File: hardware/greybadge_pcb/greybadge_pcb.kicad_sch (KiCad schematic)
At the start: 71 parts, among them J1 Conn_02x05_Row_Letter_First, J2 Conn_02x05_Row_Letter_First, J3 Conn_02x05_Row_Letter_First, J4 Conn_02x05_Row_Letter_First, SW1 SW_Push, SW2 SW_Push, SW3 SW_Push, SW4 SW_Push, SW5 SW_Push, SW6 SW_Push, SW7 SW_Push, U1 TLV62568DBV, U2 TLV62568DBV, U3 TLV73325PDBV

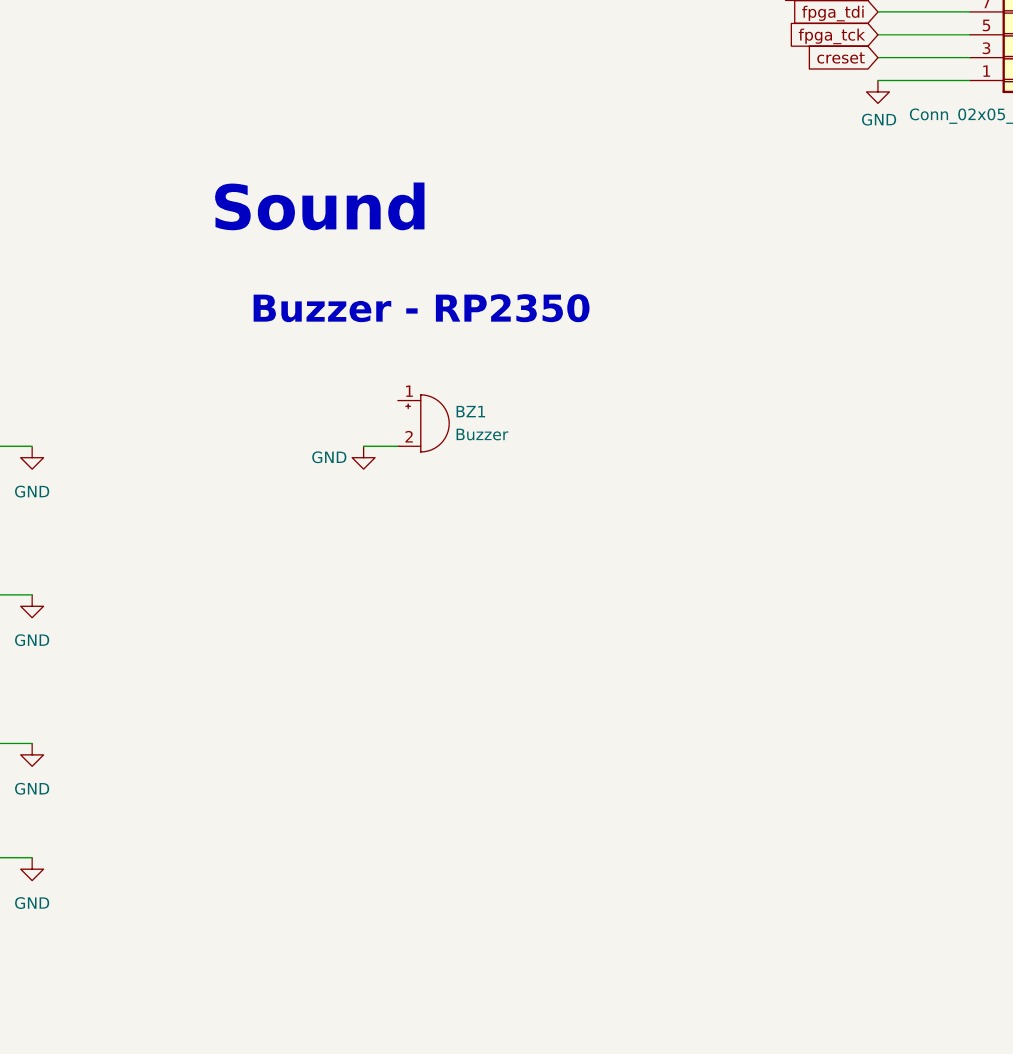
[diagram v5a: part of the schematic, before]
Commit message: feat: oled move to top sch
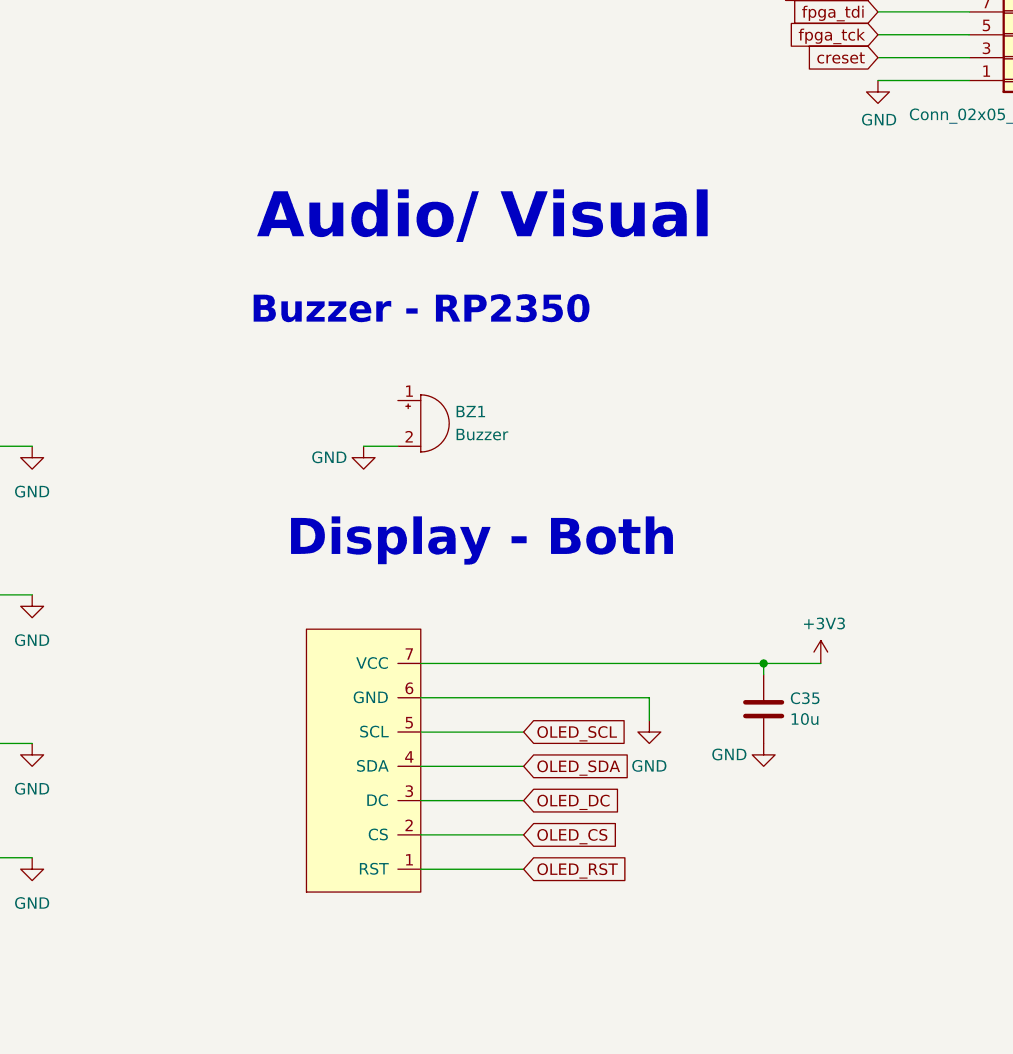
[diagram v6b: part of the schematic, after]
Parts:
- added C35: 10u, Capacitor_SMD:C_0402_1005Metric, symbol Device:C
- added GC9A1: CG9A01, custom:GC9A01, symbol maimai:CG9A01
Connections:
- net +3V3: now also C35.1, GC9A1.7 (VCC)
- net GND: now also C35.2, GC9A1.6 (GND)
- new net OLED_CS: GC9A1.2 (CS)
- new net OLED_DC: GC9A1.3 (DC)
- new net OLED_RST: GC9A1.1 (RST)
- new net OLED_SCL: GC9A1.5 (SCL)
- new net OLED_SDA: GC9A1.4 (SDA)
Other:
- note added: "Audio/ Visual"
- note added: "Display - Both"
- note removed: "Sound"

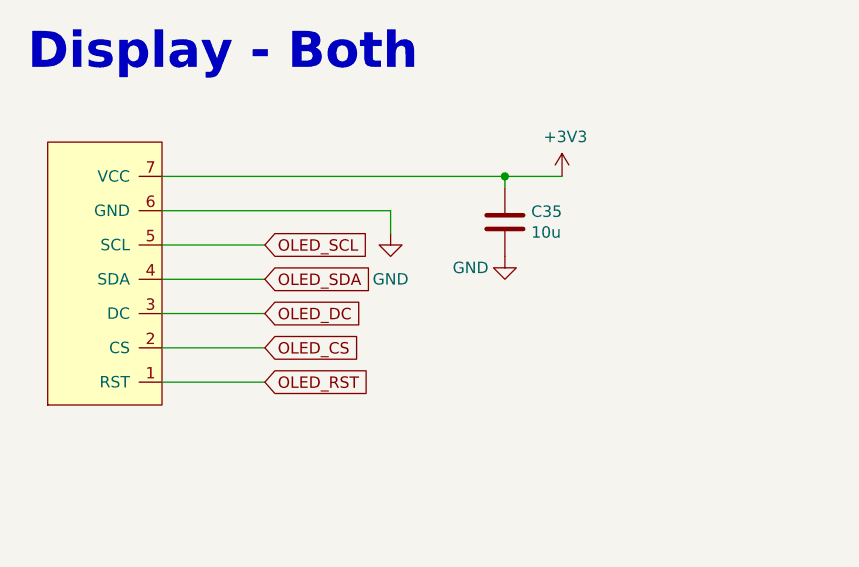
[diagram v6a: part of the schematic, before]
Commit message: feat: oled to fpga
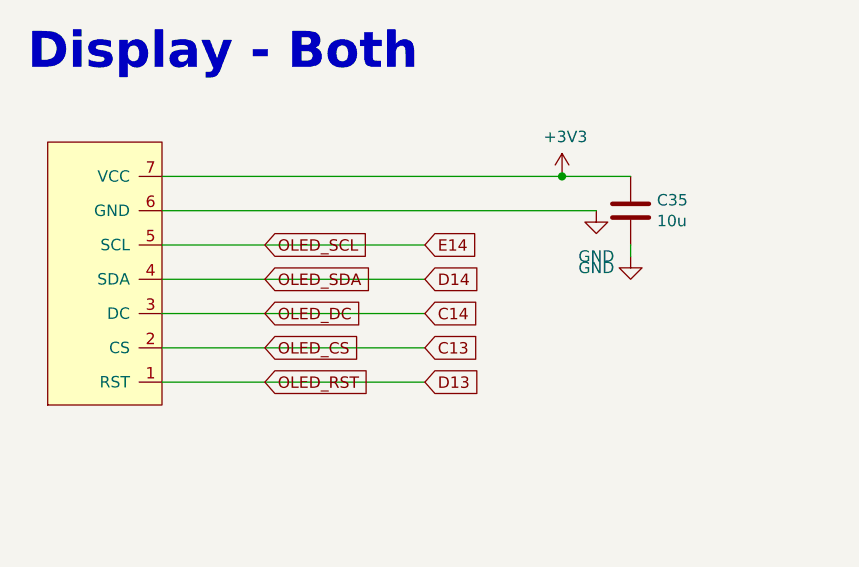
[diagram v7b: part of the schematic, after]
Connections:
- net OLED_CS renamed C13
- net OLED_DC renamed C14
- net OLED_RST renamed D13
- net OLED_SCL renamed E14
- net OLED_SDA renamed D14
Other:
- moved on the sheet: C35
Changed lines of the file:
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@@
 	)
 	(junction
+		(at 347.98 130.81)
+		(diameter 0)
+		(color 0 0 0 0)
+	)
+	(junction
 		(at 161.29 212.09)
 		(diameter 0)
@@
 	)
 	(junction
-		(at 341.63 130.81)
-		(diameter 0)
-		(color 0 0 0 0)
-	)
-	(junction
 		(at 77.47 147.32)
 		(diameter 0)
@@
 	(wire
 		(pts
-			(xy 303.53 134.62) (xy 328.93 134.62)
+			(xy 303.53 134.62) (xy 351.79 134.62)
 		)
 		(stroke
@@
 	(wire
 		(pts
-			(xy 303.53 146.05) (xy 314.96 146.05)
+			(xy 303.53 146.05) (xy 332.74 146.05)
 		)
 		(stroke
@@
 	(wire
 		(pts
-			(xy 303.53 142.24) (xy 314.96 142.24)
+			(xy 303.53 142.24) (xy 332.74 142.24)
 		)
 		(stroke
@@
 	(wire
 		(pts
-			(xy 303.53 153.67) (xy 314.96 153.67)
+			(xy 303.53 153.67) (xy 332.74 153.67)
 		)
 		(stroke
@@
 	(wire
 		(pts
-			(xy 341.63 130.81) (xy 347.98 130.81)
+			(xy 247.65 139.7) (xy 248.92 139.7)
 		)
 		(stroke
@@
 	(wire
 		(pts
-			(xy 247.65 139.7) (xy 248.92 139.7)
+			(xy 100.33 264.16) (xy 102.87 264.16)
 		)
 		(stroke
@@
 	(wire
 		(pts
-			(xy 100.33 264.16) (xy 102.87 264.16)
+			(xy 208.28 54.61) (xy 220.98 54.61)
 		)
 		(stroke
@@
 	(wire
 		(pts
-			(xy 208.28 54.61) (xy 220.98 54.61)
+			(xy 355.6 130.81) (xy 347.98 130.81)
 		)
 		(stroke
@@
 	(wire
 		(pts
-			(xy 303.53 149.86) (xy 314.96 149.86)
+			(xy 303.53 149.86) (xy 332.74 149.86)
 		)
 		(stroke
@@
 	(wire
 		(pts
-			(xy 303.53 138.43) (xy 314.96 138.43)
+			(xy 303.53 138.43) (xy 332.74 138.43)
 		)
 		(stroke
@@
 	(wire
 		(pts
-			(xy 328.93 134.62) (xy 328.93 137.16)
-		)
-		(stroke
-			(width 0)
-			(type default)
-		)
-	)
-	(wire
-		(pts
 			(xy 102.87 266.7) (xy 100.33 266.7)
 		)
@@
 	(wire
 		(pts
-			(xy 341.63 132.08) (xy 341.63 130.81)
+			(xy 45.72 241.3) (xy 59.69 241.3)
 		)
 		(stroke
@@
 	(wire
 		(pts
-			(xy 45.72 241.3) (xy 59.69 241.3)
+			(xy 355.6 138.43) (xy 355.6 139.7)
 		)
 		(stroke
@@
 	(wire
 		(pts
-			(xy 303.53 130.81) (xy 341.63 130.81)
+			(xy 303.53 130.81) (xy 347.98 130.81)
 		)
 		(stroke
@@
 			"dwBLAGgAVABKAHYAOABPAFgAeQBkAHgARQAyAHYARAAwAHcAYwBPAGoAegA3AHEAQgBnADgAdQBJ"
 			"AFQAZABBAHcAaQB3AGwAQQBMAGwAeABJAEkAawA4AEEARQBnAGoAYgBOAGIAdwB2AFEAYQB4AGkA"
-			"bQBoAEIAMwBEAFMAeQB2AHUAQQBnAGEAeAAvAE4AMwBiAEIAWABZADAAcQBIAHMAcwB5AA=="
+			"bQBoAEIAMwBEAFMAeQB2AHUAQQBnAGEAeAAvAE4AMwBiAEIAWABZADAAcQBIAHMAcwB5AGwAOQBh"
+			"AHEAUABiAFIAagBGAFYAQgBBADAAUgAyAEcAMgBvAGsAdwBMADQAcwBZAGEASAAxAE8ARABpAHcA"
+			"ZQBKAGgAaQBHAHgATQBVAEYANwBZAG8AQwBOAFEARQBpAGMARQBTAEYAQQBDAEEANABNAGcAcgBX"
+			"AHAAZwBXAGIAQwBMAGsAcwBNAHEAUQBNAHIAQQBsACsAagBqAFkANQB2AC8AVQBrAHMAWQBPAFEA"
+			"TwBBAGgAbABGAGIAYgA3AFYAQgBlAEUAWQB4AHYARABQAEQAUwBGAG4ARgByADUAKwBOAHIARgB6"
+			"AGkARwBmAFkAbgA4AEsASABzAEkANwBlADEARgB0AGYAdgBGAE8AaAA3AGgARQBDAGkAUwAxAGwA"
+			"TABSACsAKwA2AHQAWgBuADMAMwBqAHEAMQBlADMAcgBIAG4AMwA4ADAAVgBKAFUAbgB0AFkAegAr"
+			"AGMAcgB6AHIANQA1AC8AKwByAGwAbAB0AEIAaABHAFoANgBsAGoAMQBzAFEAegBXADkAQQBtAHUA"
+			"VQArAE0AcABUAHgAcwBVAGcAQgA0ADgAYgA2AHUATABmAG4ARQBQAE0AMwBLAGEARwBFAFgAbABi"
+			"AGoAOQBpAGgAWAB2AEcAOQAvAFYAdgBmAGIAMQB0AGYAZgBjAGUAOQArADQAdABvADcARgBjADUA"
+			"YQB1AG0ASAA5ACsAVgA5AEwATgA4AEkATgA1AGIAeAA0AE4ATwAwADEAagBqAE0AUQBBAFIAdQB4"
+			"AHAASABUAFAASwAxAFoAYgBCAHQATgA3AEsAUwBRAGoAaQBpAHMARgBOAEsARABJAHgAZwAyAHcA"
+			"ZQBrAFMAZABXAE4AcgA0AFMATQBmADcARgBCAHoALwA5AHgATABwAEgAMQBtADkAZQB2ACsANwBG"
+			"AHQAUgBQAGIAdQBpACsANwA0AEsAbwBsAHMAMQBlAHEAMAA3AG8AZAByAEsARgBmAGIASQB0AFQA"
+			"cwBjAFUASQBKAGkAUgAyAC8AdABSAHoAKwBDAEoAOQAvAG8AVgBuADcAcgAvAG4AdgBpAGwAVABw"
+			"AG4AegBnAGYAVABlAHYAZQBmAG8ARgBxAHAAVwBxADMATgBhAGEAdABKAC8AZQBmAFIAYgA1AEoA"
+			"TgBjADgANABpAGkAVwBaAE0ANgBVAHUAZQBOAGIASgBwAFIAUQBzAGEAbwBmAHYAKwBIAGoAZAB6"
+			"AC8AOAB2AGIAdQAvADkAMAA5AEoAYQAzAFgAdQAyAFcAZQAxAGwAOABaAE4AcQBFADYAeABYAEoA"
+			"SABDAE4AVQA4AEEARwBPAEgAVABKADgANQBOADAANQBRAGsASQBoAE4AQgBQAE8AQgBEAA=="
 		)
 	)
@@
 		)
 	)
+	(global_label "E14"
+		(shape input)
+		(at 332.74 138.43 0)
+		(fields_autoplaced yes)
+		(effects
+			(font
+				(size 1.27 1.27)
+			)
+			(justify left)
+		)
+		(property "Intersheetrefs" "${INTERSHEET_REFS}"
+			(at 339.2932 138.43 0)
+			(effects
+				(font
+					(size 1.27 1.27)
+				)
+				(justify left)
+				(hide yes)
+			)
+		)
+	)
 	(global_label "GPIO14"
 		(shape input)
@@
 		)
 	)
+	(global_label "C13"
+		(shape input)
+		(at 332.74 149.86 0)
+		(fields_autoplaced yes)
+		(effects
+			(font
+				(size 1.27 1.27)
+			)
+			(justify left)
+		)
+		(property "Intersheetrefs" "${INTERSHEET_REFS}"
+			(at 339.4142 149.86 0)
+			(effects
+				(font
+					(size 1.27 1.27)
+				)
+				(justify left)
+				(hide yes)
+			)
+		)
+	)
 	(global_label "B11"
 		(shape input)
@@
 		)
 	)
+	(global_label "D13"
+		(shape input)
+		(at 332.74 153.67 0)
+		(fields_autoplaced yes)
+		(effects
+			(font
+				(size 1.27 1.27)
+			)
+			(justify left)
+		)
+		(property "Intersheetrefs" "${INTERSHEET_REFS}"
+			(at 339.4142 153.67 0)
+			(effects
+				(font
+					(size 1.27 1.27)
+				)
+				(justify left)
+				(hide yes)
+			)
+		)
+	)
 	(global_label "B9"
 		(shape input)
@@
 		)
 	)
+	(global_label "D14"
+		(shape input)
+		(at 332.74 142.24 0)
+		(fields_autoplaced yes)
+		(effects
+			(font
+				(size 1.27 1.27)
+			)
+			(justify left)
+		)
+		(property "Intersheetrefs" "${INTERSHEET_REFS}"
+			(at 339.4142 142.24 0)
+			(effects
+				(font
+					(size 1.27 1.27)
+				)
+				(justify left)
+				(hide yes)
+			)
+		)
+	)
 	(global_label "GPIO13"
 		(shape input)
@@
 		)
 	)
+	(global_label "C14"
+		(shape input)
+		(at 332.74 146.05 0)
+		(fields_autoplaced yes)
+		(effects
+			(font
+				(size 1.27 1.27)
+			)
+			(justify left)
+		)
+		(property "Intersheetrefs" "${INTERSHEET_REFS}"
+			(at 339.4142 146.05 0)
+			(effects
+				(font
+					(size 1.27 1.27)
+				)
+				(justify left)
+				(hide yes)
+			)
+		)
+	)
 	(global_label "C3"
 		(shape input)
@@
 	(symbol
 		(lib_id "power:GND")
-		(at 328.93 137.16 0)
+		(at 351.79 134.62 0)
 		(unit 1)
 		(exclude_from_sim no)
@@
 		(fields_autoplaced yes)
 		(property "Reference" "#PWR096"
-			(at 328.93 143.51 0)
+			(at 351.79 140.97 0)
 			(effects
 				(font
@@
 		)
 		(property "Value" "GND"
-			(at 328.93 142.24 0)
+			(at 351.79 139.7 0)
 			(effects
 				(font
@@
 		)
 		(property "Footprint" ""
-			(at 328.93 137.16 0)
+			(at 351.79 134.62 0)
 			(effects
 				(font
@@
 		)
 		(property "Datasheet" ""
-			(at 328.93 137.16 0)
+			(at 351.79 134.62 0)
 			(effects
 				(font
@@
 		)
 		(property "Description" ""
-			(at 328.93 137.16 0)
+			(at 351.79 134.62 0)
 			(effects
 				(font
@@
 	(symbol
 		(lib_id "Device:C")
-		(at 341.63 135.89 0)
+		(at 355.6 134.62 0)
 		(unit 1)
 		(exclude_from_sim no)
@@
 		(dnp no)
 		(property "Reference" "C35"
-			(at 344.551 134.7216 0)
+			(at 358.521 133.4516 0)
 			(effects
 				(font
@@
 		)
 		(property "Value" "10u"
-			(at 344.551 137.033 0)
+			(at 358.521 135.763 0)
 			(effects
 				(font
@@
 		)
 		(property "Footprint" "Capacitor_SMD:C_0402_1005Metric"
-			(at 342.5952 139.7 0)
+			(at 356.5652 138.43 0)
 			(effects
 				(font
@@
 		)
 		(property "Datasheet" "~"
-			(at 341.63 135.89 0)
+			(at 355.6 134.62 0)
 			(effects
 				(font
@@
 		)
 		(property "Description" ""
-			(at 341.63 135.89 0)
+			(at 355.6 134.62 0)
 			(effects
 				(font
@@
 	(symbol
 		(lib_id "power:GND")
-		(at 341.63 139.7 0)
+		(at 355.6 139.7 0)
 		(unit 1)
 		(exclude_from_sim no)
@@
 		(dnp no)
 		(property "Reference" "#PWR097"
-			(at 341.63 146.05 0)
+			(at 355.6 146.05 0)
 			(effects
 				(font
@@
 		)
 		(property "Value" "GND"
-			(at 337.82 140.97 0)
+			(at 351.79 140.97 0)
 			(effects
 				(font
@@
 		)
 		(property "Footprint" ""
-			(at 341.63 139.7 0)
+			(at 355.6 139.7 0)
 			(effects
 				(font
@@
 		)
 		(property "Datasheet" ""
-			(at 341.63 139.7 0)
+			(at 355.6 139.7 0)
 			(effects
 				(font
@@
 		)
 		(property "Description" ""
-			(at 341.63 139.7 0)
+			(at 355.6 139.7 0)
 			(effects
 				(font
